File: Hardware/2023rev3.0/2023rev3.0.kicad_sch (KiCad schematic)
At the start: 112 parts, among them U6 INA195

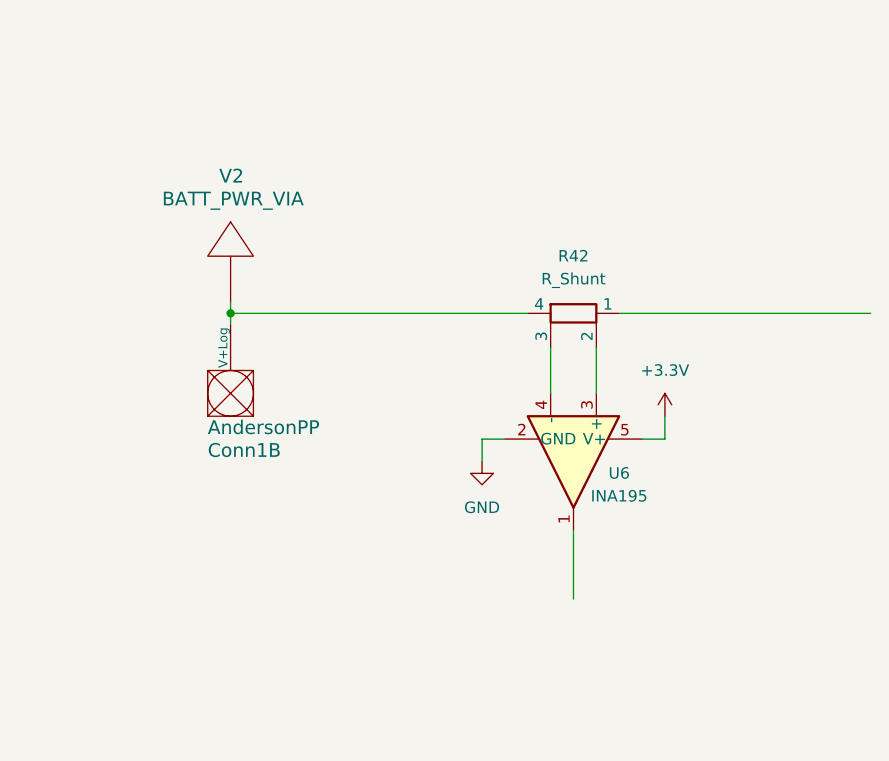
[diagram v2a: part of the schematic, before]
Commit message: Removed shunt
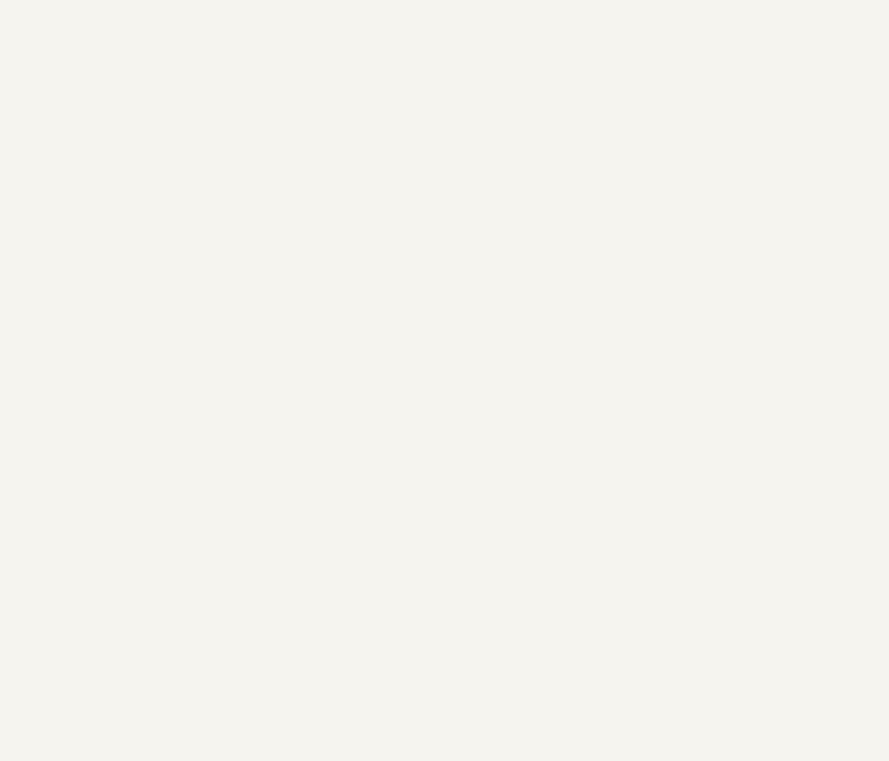
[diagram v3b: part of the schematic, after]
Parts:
- removed Conn1: AndersonPP, MRDT_Connectors:Square_Anderson_2_V_Side_By_Side_PV, symbol MRDT_Connectors:AndersonPP
- removed R42: R_Shunt, symbol Device:R_Shunt
- removed U6: INA195, Package_TO_SOT_SMD:SOT-23-6, symbol Amplifier_Current:INA195
- removed V2: BATT_PWR_VIA, MRDT_Drill_Holes:BATT_PWR_VIA, symbol MRDT_Drill_Holes:BATT_PWR_VIA
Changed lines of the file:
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@@
   (junction (at 137.16 142.24) (diameter 0) (color 0 0 0 0)
   )
-  (junction (at 465.455 205.74) (diameter 0) (color 0 0 0 0)
-  )
   (junction (at 268.605 297.815) (diameter 0) (color 0 0 0 0)
   )
@@
     (stroke (width 0) (type default) (color 0 0 0 0))
   )
-  (wire (pts (xy 513.715 217.17) (xy 513.715 219.71))
-    (stroke (width 0) (type default) (color 0 0 0 0))
-  )
   (wire (pts (xy 118.11 118.11) (xy 121.92 118.11))
     (stroke (width 0) (type default) (color 0 0 0 0))
   )
-  (wire (pts (xy 506.095 209.55) (xy 506.095 214.63))
-    (stroke (width 0) (type default) (color 0 0 0 0))
-  )
   (wire (pts (xy 152.4 165.1) (xy 152.4 173.355))
     (stroke (width 0) (type default) (color 0 0 0 0))
@@
     (stroke (width 0) (type default) (color 0 0 0 0))
   )
-  (wire (pts (xy 501.015 209.55) (xy 501.015 214.63))
-    (stroke (width 0) (type default) (color 0 0 0 0))
-  )
   (wire (pts (xy 281.305 315.595) (xy 281.305 320.675))
     (stroke (width 0) (type default) (color 0 0 0 0))
@@
     (stroke (width 0) (type default) (color 0 0 0 0))
   )
-  (wire (pts (xy 465.455 205.74) (xy 465.455 207.01))
-    (stroke (width 0) (type default) (color 0 0 0 0))
-  )
   (wire (pts (xy 125.73 191.77) (xy 121.92 191.77))
     (stroke (width 0) (type default) (color 0 0 0 0))
@@
     (stroke (width 0) (type default) (color 0 0 0 0))
   )
-  (wire (pts (xy 465.455 205.74) (xy 498.475 205.74))
-    (stroke (width 0) (type default) (color 0 0 0 0))
-  )
   (polyline (pts (xy 231.775 224.155) (xy 280.035 224.155))
     (stroke (width 0) (type default) (color 0 0 0 0))
@@
     (stroke (width 0) (type default) (color 0 0 0 0))
   )
-  (wire (pts (xy 508.635 205.74) (xy 536.575 205.74))
-    (stroke (width 0) (type default) (color 0 0 0 0))
-  )
   (polyline (pts (xy 372.745 305.435) (xy 244.475 305.435))
     (stroke (width 0) (type default) (color 0 0 0 0))
@@
     (stroke (width 0) (type default) (color 0 0 0 0))
   )
-  (wire (pts (xy 513.715 219.71) (xy 511.175 219.71))
-    (stroke (width 0) (type default) (color 0 0 0 0))
-  )
   (polyline (pts (xy 386.08 88.9) (xy 392.43 88.9))
     (stroke (width 0) (type default) (color 0 0 0 0))
@@
     (stroke (width 0) (type default) (color 0 0 0 0))
   )
-  (wire (pts (xy 495.935 219.71) (xy 493.395 219.71))
-    (stroke (width 0) (type default) (color 0 0 0 0))
-  )
   (wire (pts (xy 137.16 198.12) (xy 137.16 205.74))
     (stroke (width 0) (type default) (color 0 0 0 0))
@@
     (stroke (width 0) (type default) (color 0 0 0 0))
   )
-  (wire (pts (xy 503.555 229.87) (xy 503.555 237.49))
-    (stroke (width 0) (type default) (color 0 0 0 0))
-  )
   (polyline (pts (xy 392.43 119.38) (xy 421.64 119.38))
     (stroke (width 0) (type default) (color 0 0 0 0))
@@
     (stroke (width 0) (type default) (color 0 0 0 0))
   )
-  (wire (pts (xy 493.395 219.71) (xy 493.395 222.25))
-    (stroke (width 0) (type default) (color 0 0 0 0))
-  )
   (wire (pts (xy 262.89 237.49) (xy 264.16 237.49))
     (stroke (width 0) (type default) (color 0 0 0 0))
@@
     (stroke (width 0) (type default) (color 0 0 0 0))
   )
-  (wire (pts (xy 465.455 204.47) (xy 465.455 205.74))
-    (stroke (width 0) (type default) (color 0 0 0 0))
-  )
   (wire (pts (xy 321.945 273.685) (xy 324.485 273.685))
     (stroke (width 0) (type default) (color 0 0 0 0))
@@
     (pin "2")
   )
-  (symbol (lib_id "Amplifier_Current:INA195") (at 503.555 222.25 270) (unit 1)
-    (in_bom yes) (on_board yes)
-    (property "Reference" "U6" (id 0) (at 508.635 223.52 90))
-    (property "Value" "INA195" (id 1) (at 508.635 226.06 90))
-    (property "Footprint" "Package_TO_SOT_SMD:SOT-23-6" (id 2) (at 503.555 222.25 0)
-      (effects (font (size 1.27 1.27)) hide)
-    )
-    (property "Datasheet" "http://www.ti.com/lit/ds/symlink/ina193.pdf" (id 3) (at 503.555 222.25 0)
-      (effects (font (size 1.27 1.27)) hide)
-    )
-    (pin "1")
-    (pin "2")
-    (pin "3")
-    (pin "4")
-    (pin "5")
-  )
   (symbol (lib_id "power:+3.3V") (at 395.605 149.86 0) (unit 1)
     (in_bom yes) (on_board yes)
@@
     (pin "2")
   )
-  (symbol (lib_id "power:+3.3V") (at 513.715 217.17 0) (unit 1)
-    (in_bom yes) (on_board yes) (fields_autoplaced)
-    (property "Reference" "#PWR030" (id 0) (at 513.715 220.98 0)
-      (effects (font (size 1.27 1.27)) hide)
-    )
-    (property "Value" "+3.3V" (id 1) (at 513.715 212.09 0))
-    (property "Footprint" "" (id 2) (at 513.715 217.17 0)
-      (effects (font (size 1.27 1.27)) hide)
-    )
-    (property "Datasheet" "" (id 3) (at 513.715 217.17 0)
-      (effects (font (size 1.27 1.27)) hide)
-    )
-    (pin "1")
-  )
   (symbol (lib_id "MRDT_Connectors:AndersonPP") (at 225.425 302.895 90) (unit 2)
     (in_bom yes) (on_board yes)
@@
     (pin "2")
   )
-  (symbol (lib_id "power:GND") (at 493.395 222.25 0) (unit 1)
-    (in_bom yes) (on_board yes) (fields_autoplaced)
-    (property "Reference" "#PWR029" (id 0) (at 493.395 228.6 0)
-      (effects (font (size 1.27 1.27)) hide)
-    )
-    (property "Value" "GND" (id 1) (at 493.395 227.33 0))
-    (property "Footprint" "" (id 2) (at 493.395 222.25 0)
-      (effects (font (size 1.27 1.27)) hide)
-    )
-    (property "Datasheet" "" (id 3) (at 493.395 222.25 0)
-      (effects (font (size 1.27 1.27)) hide)
-    )
-    (pin "1")
-  )
   (symbol (lib_id "Device:R") (at 129.54 63.5 270) (mirror x) (unit 1)
     (in_bom yes) (on_board yes)
@@
     (pin "1")
   )
-  (symbol (lib_id "MRDT_Drill_Holes:BATT_PWR_VIA") (at 465.455 199.39 0) (unit 1)
-    (in_bom yes) (on_board yes)
-    (property "Reference" "V2" (id 0) (at 464.185 190.5 0)
-      (effects (font (size 1.524 1.524)) (justify left))
-    )
-    (property "Value" "BATT_PWR_VIA" (id 1) (at 457.835 193.04 0)
-      (effects (font (size 1.524 1.524)) (justify left))
-    )
-    (property "Footprint" "MRDT_Drill_Holes:BATT_PWR_VIA" (id 2) (at 465.455 199.39 0)
-      (effects (font (size 1.524 1.524)) hide)
-    )
-    (property "Datasheet" "" (id 3) (at 465.455 199.39 0)
-      (effects (font (size 1.524 1.524)) hide)
-    )
-    (pin "1")
-  )
   (symbol (lib_id "Device:C_Polarized_US") (at 328.295 319.405 0) (unit 1)
     (in_bom yes) (on_board yes)
@@
     (pin "2")
   )
-  (symbol (lib_id "MRDT_Connectors:AndersonPP") (at 467.995 217.17 90) (unit 2)
-    (in_bom yes) (on_board yes)
-    (property "Reference" "Conn1" (id 0) (at 462.915 220.98 90)
-      (effects (font (size 1.524 1.524)) (justify right))
-    )
-    (property "Value" "AndersonPP" (id 1) (at 462.915 218.44 90)
-      (effects (font (size 1.524 1.524)) (justify right))
-    )
-    (property "Footprint" "MRDT_Connectors:Square_Anderson_2_V_Side_By_Side_PV" (id 2) (at 481.965 220.98 0)
-      (effects (font (size 1.524 1.524)) hide)
-    )
-    (property "Datasheet" "" (id 3) (at 481.965 220.98 0)
-      (effects (font (size 1.524 1.524)) hide)
-    )
-    (pin "1")
-    (pin "2")
-    (pin "3")
-    (pin "4")
-    (pin "1")
-  )
   (symbol (lib_id "Connector_Generic:Conn_01x02") (at 392.43 101.6 180) (unit 1)
     (in_bom yes) (on_board yes)
@@
     (pin "2")
   )
-  (symbol (lib_id "Device:R_Shunt") (at 503.555 205.74 270) (unit 1)
-    (in_bom yes) (on_board yes) (fields_autoplaced)
-    (property "Reference" "R42" (id 0) (at 503.555 199.39 90))
-    (property "Value" "R_Shunt" (id 1) (at 503.555 201.93 90))
-    (property "Footprint" "" (id 2) (at 503.555 203.962 90)
-      (effects (font (size 1.27 1.27)) hide)
-    )
-    (property "Datasheet" "~" (id 3) (at 503.555 205.74 0)
-      (effects (font (size 1.27 1.27)) hide)
-    )
-    (pin "1")
-    (pin "2")
-    (pin "3")
-    (pin "4")
-  )
   (symbol (lib_id "Device:R") (at 129.54 124.46 270) (mirror x) (unit 1)
     (in_bom yes) (on_board yes)
@@
   )
   (symbol_instances
-    (path "/60572072-b540-43e6-a72a-8bb7a99cfff7"
-      (reference "#PWR029") (unit 1) (value "GND") (footprint "")
-    )
-    (path "/47106ca1-f6a6-4988-aaaf-0556c1671c68"
-      (reference "#PWR030") (unit 1) (value "+3.3V") (footprint "")
-    )
     (path "/1a1d5f32-11ed-41c2-a08a-a3e5905daa62"
       (reference "#PWR?") (unit 1) (value "GND") (footprint "")
@@
       (reference "C?") (unit 1) (value "0.1uF") (footprint "Capacitor_SMD:C_0603_1608Metric_Pad1.08x0.95mm_HandSolder")
     )
-    (path "/b83991ac-a679-4e2d-9c43-3fb45895fb02"
-      (reference "Conn1") (unit 2) (value "AndersonPP") (footprint "MRDT_Connectors:Square_Anderson_2_V_Side_By_Side_PV")
-    )
     (path "/9ff307e2-adac-4fa6-b84d-a0ce3748300c"
       (reference "Conn?") (unit 1) (value "AndersonPP") (footprint "MRDT_Connectors:Square_Anderson_2_V_Side_By_Side")
@@
       (reference "Q?") (unit 1) (value "BSS138") (footprint "Package_TO_SOT_SMD:SOT-23")
     )
-    (path "/f13649bd-37f4-43b1-a999-5ffc1b5ef923"
-      (reference "R42") (unit 1) (value "R_Shunt") (footprint "")
-    )
     (path "/0d4d29c2-bb94-4f53-a763-b656b35c7f05"
       (reference "R?") (unit 1) (value "3.3k") (footprint "Resistor_SMD:R_0603_1608Metric_Pad0.98x0.95mm_HandSolder")
@@
       (reference "R?") (unit 1) (value "100") (footprint "Resistor_SMD:R_0603_1608Metric_Pad0.98x0.95mm_HandSolder")
     )
-    (path "/206e7826-bd29-4621-aab0-15fa3998f35f"
-      (reference "U6") (unit 1) (value "INA195") (footprint "Package_TO_SOT_SMD:SOT-23-6")
-    )
     (path "/0dd0b934-38d9-42e4-b507-f3fc5f2c1ec1"
       (reference "U?") (unit 1) (value "Opamp_Dual") (footprint "Package_SO:SO-8_3.9x4.9mm_P1.27mm")
@@
       (reference "U?") (unit 3) (value "Opamp_Dual") (footprint "Package_SO:SO-8_3.9x4.9mm_P1.27mm")
     )
-    (path "/805edeac-d29f-4dcf-8661-803e921f6396"
-      (reference "V2") (unit 1) (value "BATT_PWR_VIA") (footprint "MRDT_Drill_Holes:BATT_PWR_VIA")
-    )
     (path "/07448738-0187-4896-96ec-30b624e144b2"

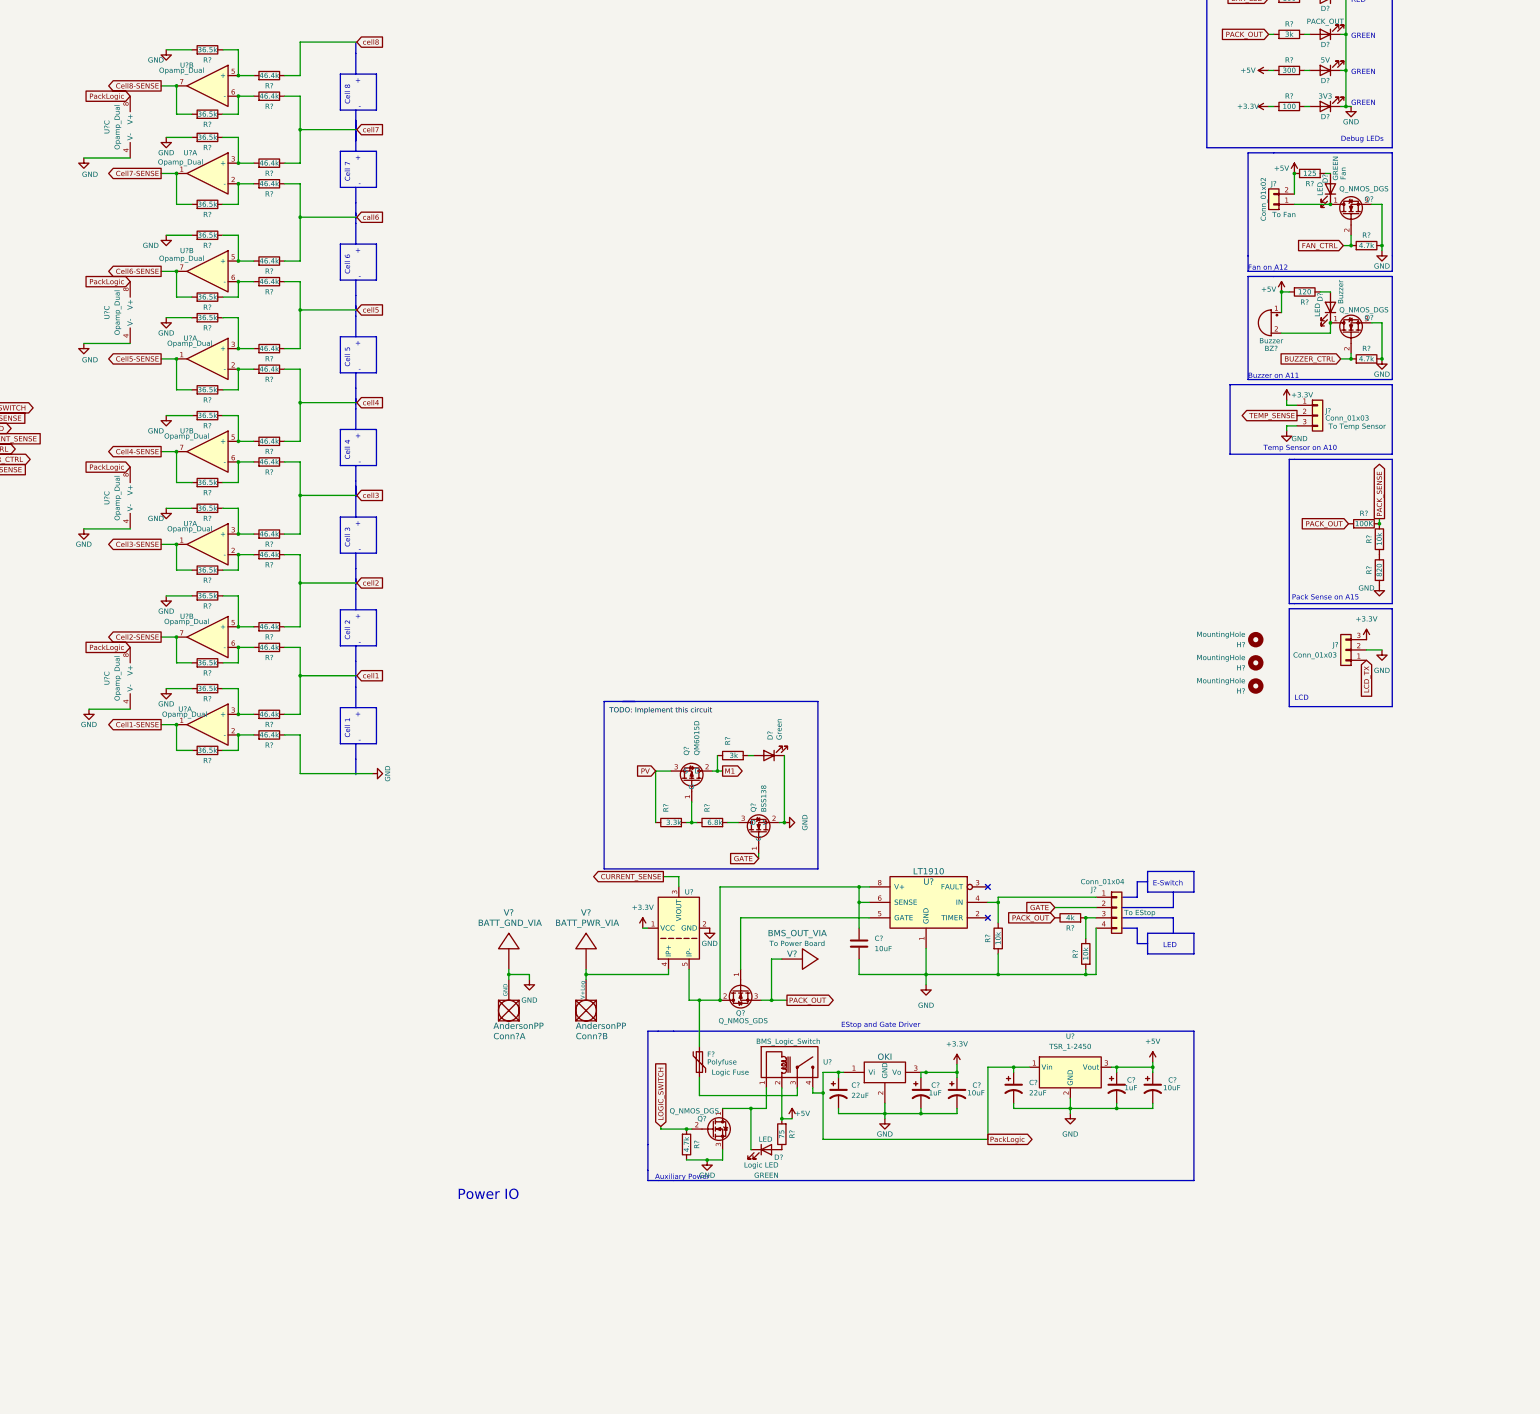
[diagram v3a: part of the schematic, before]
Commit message: started adding caps
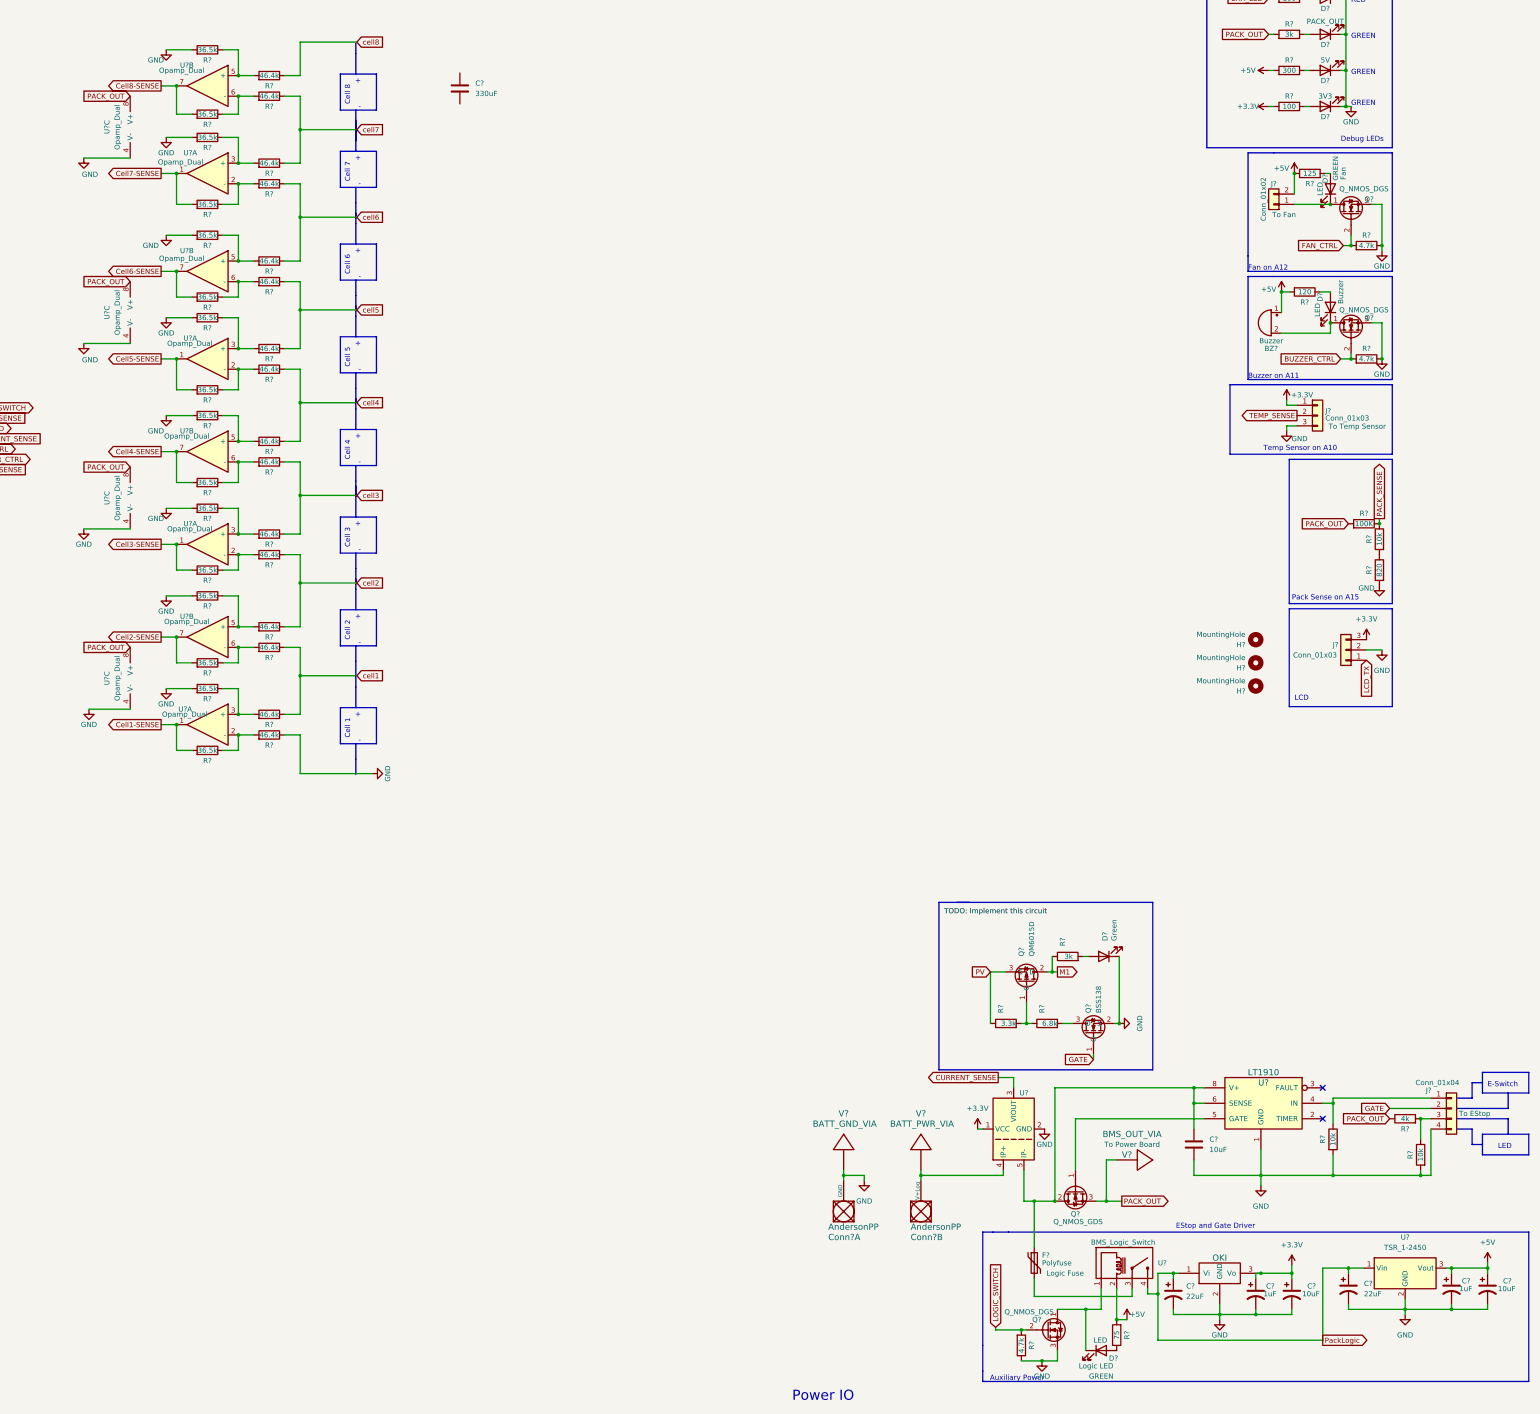
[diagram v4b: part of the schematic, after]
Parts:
- added C?: 330uF, symbol Device:C
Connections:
- net PACK_OUT: now also U?.8 (V+), U?.8 (V+), U?.8 (V+), U?.8 (V+)
- net PackLogic: no longer U?.8 (V+), U?.8 (V+), U?.8 (V+), U?.8 (V+)
- net call6: no longer R?.1, R?.1
- new net cell6: R?.1, R?.1
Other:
- moved on the sheet: C?, Conn?A, Conn?B, D?, F?, J?, Q?, R?, U?, V?
